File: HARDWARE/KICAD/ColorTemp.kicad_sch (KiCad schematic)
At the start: 27 parts, among them J1 POWER, J2 EXPANSION, SW1 USER, SW2 ~{RESET}, U1 CH32V003F4U6, U2 MCP9700A

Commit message: Finished schematic.
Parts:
- J1: JLCPCB (none) -> C2927029; Manufacturer (none) -> DEALON; Part Number (none) -> USB-TYPE-C-009
- R3, R4, R5: value 1K 1% -> 220R 1%; symbol ColorTemp:R0402 1K 1% 50V 62.5mW -> ColorTemp:R0402 220R 1% 50V 62.5mW; JLCPCB C11702 -> C25091; Part Number 0402WGF1001TCE -> 0402WGF2200TCE
- SW1, SW2: symbol ColorTemp: EVQP7A01P -> ColorTemp:EVQP7A01P; Part Number EVQP7A01P -> EVQP7A01P
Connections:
- net CC1: now reaches J1.A5 (CC1), R2.1
- net CC2: now reaches J1.B5 (CC2), R1.1
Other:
- note removed: "CHANGE TO 100R 0402"
- moved on the sheet: C1, C2, C3, C4, D1, FID1, FID2, FID3, H1, H2, H3, H4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

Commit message: Generated BOM and placement files. Updated detail on 220R in component library.
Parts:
- R3, R4, R5: JLCPCB C25091 -> C25091; Part Number 0402WGF2200TCE -> 0402WGF2200TCE
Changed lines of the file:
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@@
 			)
 		)
-		(property "Part Number" " 0402WGF2200TCE"
+		(property "Part Number" "0402WGF2200TCE"
 			(at 114.3 100.33 0)
 			(effects
@@
 			)
 		)
-		(property "JLCPCB" " C25091"
+		(property "JLCPCB" "C25091"
 			(at 114.3 100.33 0)
 			(effects
@@
 			)
 		)
-		(property "Part Number" " 0402WGF2200TCE"
+		(property "Part Number" "0402WGF2200TCE"
 			(at 114.3 64.77 0)
 			(effects
@@
 			)
 		)
-		(property "JLCPCB" " C25091"
+		(property "JLCPCB" "C25091"
 			(at 114.3 64.77 0)
 			(effects
@@
 			)
 		)
-		(property "Part Number" " 0402WGF2200TCE"
+		(property "Part Number" "0402WGF2200TCE"
 			(at 160.02 72.39 0)
 			(effects
@@
 			)
 		)
-		(property "JLCPCB" " C25091"
+		(property "JLCPCB" "C25091"
 			(at 160.02 72.39 0)
 			(effects

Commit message: Generated BOM and Pick and Place files.
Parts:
- U1: JLCPCB (none) -> C5299908; Manufacturer (none) -> WCH; Part Number (none) -> CH32V003F4U6
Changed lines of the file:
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@@
+			)
+		)
+		(property "Part Number" "CH32V003F4U6"
+			(at 139.7 74.93 0)
+			(effects
+				(font
+					(size 1.27 1.27)
+				)
+				(hide yes)
+			)
+		)
+		(property "Manufacturer" "WCH"
+			(at 139.7 74.93 0)
+			(effects
+				(font
+					(size 1.27 1.27)
+				)
+				(hide yes)
+			)
+		)
+		(property "JLCPCB" "C5299908"
+			(at 139.7 74.93 0)
+			(effects
+				(font
+					(size 1.27 1.27)
+				)
+				(hide yes)
 			)
 		)

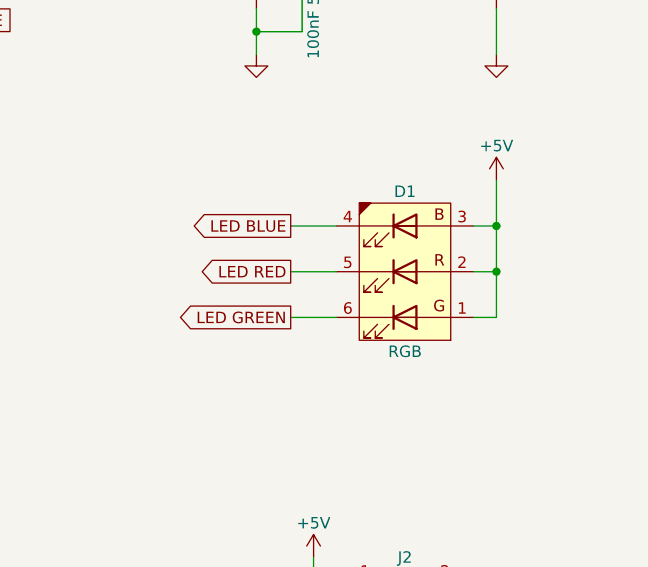
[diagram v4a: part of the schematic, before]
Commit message: Had to replace de LED because it was not in Economic fabrication at JLC.
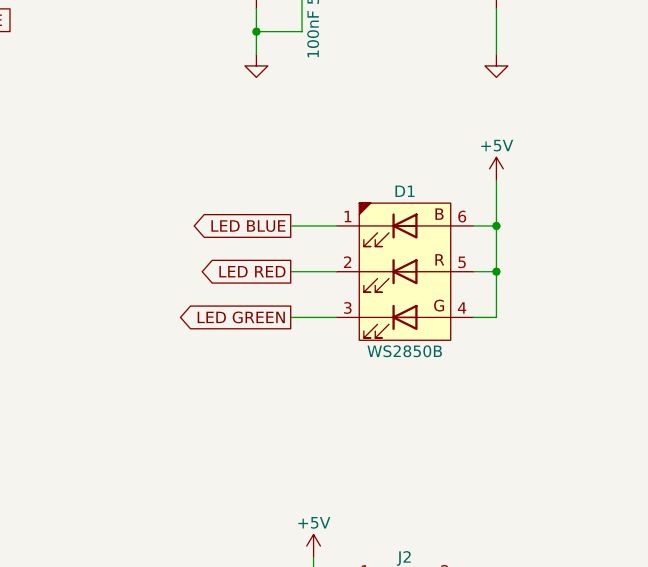
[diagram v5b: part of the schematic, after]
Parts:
- removed D1: RGB, ColorTemp:LED_RGB_5050-6, symbol ColorTemp:LED RGB 5050
- added D1: WS2850B, ColorTemp:WS2850B, symbol ColorTemp:WS2850B
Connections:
- net +5V: now also D1.4 (K), D1.5 (K), D1.6 (K)
- net LED BLUE: now also D1.1 (A)
- net LED GREEN: now also D1.3 (A)
- net LED RED: now also D1.2 (A)
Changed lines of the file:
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@@
-	)
-	(symbol
-		(lib_id "ColorTemp:LED RGB 5050")
-		(at 232.41 100.33 180)
-		(unit 1)
-		(exclude_from_sim no)
-		(in_bom yes)
-		(on_board yes)
-		(dnp no)
-		(property "Reference" "D1"
-			(at 232.41 91.44 0)
-			(effects
-				(font
-					(size 1.27 1.27)
-				)
-			)
-		)
-		(property "Value" "RGB"
-			(at 232.41 109.22 0)
-			(effects
-				(font
-					(size 1.27 1.27)
-				)
-			)
-		)
-		(property "Footprint" "ColorTemp:LED_RGB_5050-6"
-			(at 232.41 100.33 0)
-			(effects
-				(font
-					(size 1.27 1.27)
-				)
-				(hide yes)
-			)
-		)
-		(property "Datasheet" "https://jlcpcb.com/api/file/downloadByFileSystemAccessId/8558290373673050112"
-			(at 232.41 87.63 0)
-			(effects
-				(font
-					(size 1.27 1.27)
-				)
-				(hide yes)
-			)
-		)
-		(property "Description" "Light emitting diode"
-			(at 230.886 89.662 0)
-			(effects
-				(font
-					(size 1.27 1.27)
-				)
-				(hide yes)
-			)
-		)
-		(property "Part Number" " TC5050RGBF08-3CJH-AF53A"
-			(at 232.41 92.71 0)
-			(effects
-				(font
-					(size 1.27 1.27)
-				)
-				(hide yes)
-			)
-		)
-		(property "Manufacturer" " TCWIN"
-			(at 232.664 89.662 0)
-			(effects
-				(font
-					(size 1.27 1.27)
-				)
-				(hide yes)
-			)
-		)
-		(property "JLCPCB" "C784540"
-			(at 232.41 91.44 0)
-			(effects
-				(font
-					(size 1.27 1.27)
-				)
-				(hide yes)
-			)
-		)
-		(pin "4"
-		)
-		(pin "1"
-		)
-		(pin "3"
-		)
-		(pin "6"
-		)
-		(pin "2"
-		)
-		(pin "5"
-		)
-		(instances
-			(project ""
-				(path "/b6e9e66b-bd82-486a-892a-2943c5ea8e95"
-					(reference "D1")
-					(unit 1)
-				)
-			)
-		)
 	)
 	(symbol
@@
 					(unit 1)
 				)
+			)
+		)
+	)
+	(symbol
+		(lib_id "ColorTemp:WS2850B")
+		(at 232.41 100.33 0)
+		(unit 1)
+		(exclude_from_sim no)
+		(in_bom yes)
+		(on_board yes)
+		(dnp no)
+		(property "Reference" "D1"
+			(at 232.41 91.44 0)
+			(effects
+				(font
+					(size 1.27 1.27)
+				)
+			)
+		)
+		(property "Value" "WS2850B"
+			(at 232.41 109.22 0)
+			(effects
+				(font
+					(size 1.27 1.27)
+				)
+			)
+		)
+		(property "Footprint" "ColorTemp:WS2850B"
+			(at 232.664 111.76 0)
+			(effects
+				(font
+					(size 1.27 1.27)
+				)
+				(hide yes)
+			)
+		)
+		(property "Datasheet" "https://jlcpcb.com/api/file/downloadByFileSystemAccessId/8590906233161396224"
+			(at 232.41 111.76 0)
+			(effects
+				(font
+					(size 1.27 1.27)
+				)
+				(hide yes)
+			)
+		)
+		(property "Description" "Light emitting diode"
+			(at 232.41 111.76 0)
+			(effects
+				(font
+					(size 1.27 1.27)
+				)
+				(hide yes)
+			)
+		)
+		(property "Part Number" "WS2850B"
+			(at 232.41 111.76 0)
+			(effects
+				(font
+					(size 1.27 1.27)
+				)
+				(hide yes)
+			)
+		)
+		(property "Manufacturer" "Worldsemi"
+			(at 232.41 111.76 0)
+			(effects
+				(font
+					(size 1.27 1.27)
+				)
+				(hide yes)
+			)
+		)
+		(property "JLCPCB" "C4154880"
+			(at 232.41 111.76 0)
+			(effects
+				(font
+					(size 1.27 1.27)
+				)
+				(hide yes)
+			)
+		)
+		(pin "5"
+		)
+		(pin "1"
+		)
+		(pin "2"
+		)
+		(pin "3"
+		)
+		(pin "4"
+		)
+		(pin "6"
+		)
+		(instances
+			(project ""
+				(path "/b6e9e66b-bd82-486a-892a-2943c5ea8e95"
+					(reference "D1")
+					(unit 1)
+				)

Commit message: Fixed incorrect PN on 5.1K resistors.
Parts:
- R1, R2, R6, R7, R8, R9: JLCPCB C11702 -> C25905; Part Number 0402WGF1001TCE -> 0402WGF5101TCE
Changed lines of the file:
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@@
 			)
 		)
-		(property "Part Number" "0402WGF1001TCE"
+		(property "Part Number" "0402WGF5101TCE"
 			(at 114.3 88.9 0)
 			(effects
@@
 			)
 		)
-		(property "JLCPCB" "C11702"
+		(property "JLCPCB" "C25905"
 			(at 114.3 88.9 0)
 			(effects
@@
 			)
 		)
-		(property "Part Number" "0402WGF1001TCE"
+		(property "Part Number" "0402WGF5101TCE"
 			(at 62.23 69.85 0)
 			(effects
@@
 			)
 		)
-		(property "JLCPCB" "C11702"
+		(property "JLCPCB" "C25905"
 			(at 62.23 69.85 0)
 			(effects
@@
 			)
 		)
-		(property "Part Number" "0402WGF1001TCE"
+		(property "Part Number" "0402WGF5101TCE"
 			(at 54.61 69.85 0)
 			(effects
@@
 			)
 		)
-		(property "JLCPCB" "C11702"
+		(property "JLCPCB" "C25905"
 			(at 54.61 69.85 0)
 			(effects
@@
 			)
 		)
-		(property "Part Number" "0402WGF1001TCE"
+		(property "Part Number" "0402WGF5101TCE"
 			(at 106.68 88.9 0)
 			(effects
@@
 			)
 		)
-		(property "JLCPCB" "C11702"
+		(property "JLCPCB" "C25905"
 			(at 106.68 88.9 0)
 			(effects
@@
 			)
 		)
-		(property "Part Number" "0402WGF1001TCE"
+		(property "Part Number" "0402WGF5101TCE"
 			(at 215.9 52.07 0)
 			(effects
@@
 			)
 		)
-		(property "JLCPCB" "C11702"
+		(property "JLCPCB" "C25905"
 			(at 215.9 52.07 0)
 			(effects
@@
 			)
 		)
-		(property "Part Number" "0402WGF1001TCE"
+		(property "Part Number" "0402WGF5101TCE"
 			(at 242.57 52.07 0)
 			(effects
@@
 			)
 		)
-		(property "JLCPCB" "C11702"
+		(property "JLCPCB" "C25905"
 			(at 242.57 52.07 0)
 			(effects
